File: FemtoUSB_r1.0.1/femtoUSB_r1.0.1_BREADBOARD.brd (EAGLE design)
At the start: 40.6 x 20.3 mm, 32 parts, among them IC1 ATSAMD21E18A-MUT

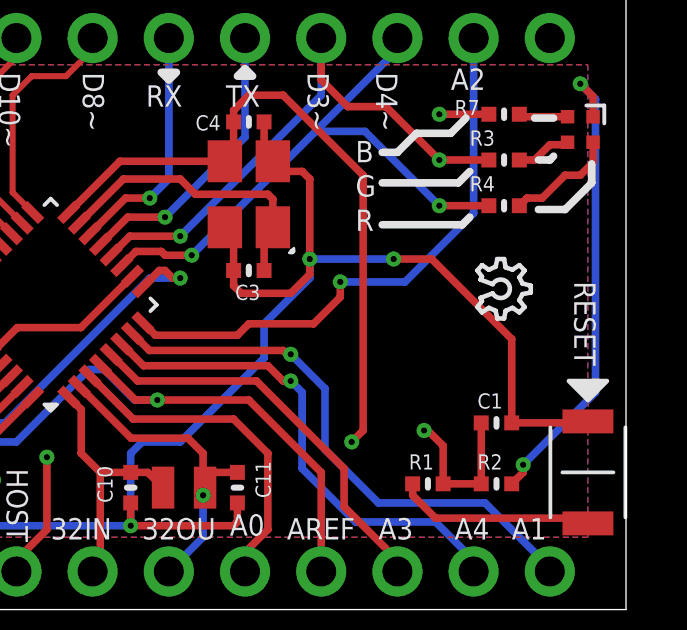
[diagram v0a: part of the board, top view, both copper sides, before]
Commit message: Updating FemtoUSB r1.0.1 w/ RGB. Silkscreen updated to reflect Arduino pin assignments
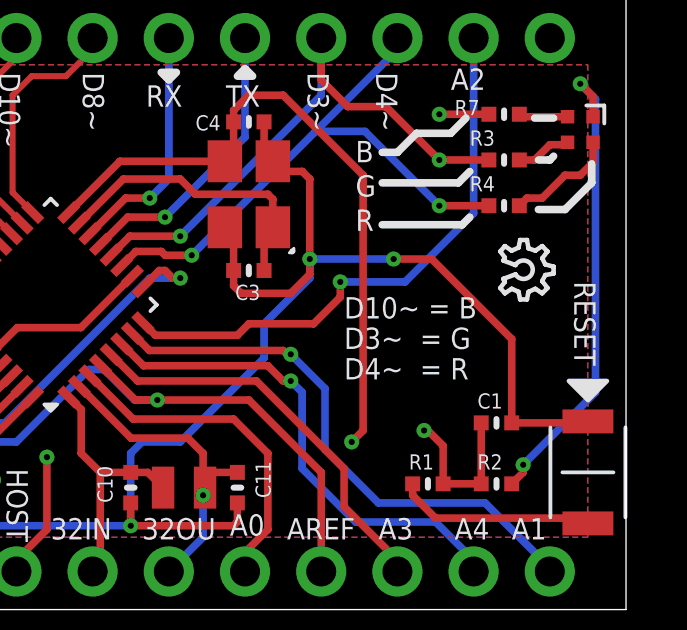
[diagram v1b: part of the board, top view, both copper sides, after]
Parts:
- moved OSH_LOGO 0.99 mm to (36.4, 12.3)
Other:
- board text added: "D10~ = B"
- board text added: "D3~ = G"
- board text added: "D4~ = R"
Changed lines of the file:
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@@
 <wire x1="38.1" y1="14.986" x2="38.227" y2="15.113" width="0.254" layer="25"/>
 <wire x1="37.592" y1="16.383" x2="38.227" y2="16.383" width="0.254" layer="25"/>
+<text x="31.242" y="10.414" size="0.7112" layer="25" font="vector" ratio="20" rot="SR0" align="top-left">D10~ = B</text>
+<text x="31.242" y="9.398" size="0.7112" layer="25" font="vector" ratio="20" rot="SR0" align="top-left">D3~  = G</text>
+<text x="31.242" y="8.382" size="0.7112" layer="25" font="vector" ratio="20" rot="SR0" align="top-left">D4~  = R</text>
 </plain>
 <attributes>
@@
 <attribute name="VALUE" x="11.303" y="14.8272" size="0.4572" layer="27" font="vector" ratio="20"/>
 </element>
-<element name="OSH_LOGO" library="ohw-logo" package="OSHW_6X70_NOTEXT" value="" x="35.687" y="11.684" rot="R270"/>
+<element name="OSH_LOGO" library="ohw-logo" package="OSHW_6X70_NOTEXT" value="" x="36.449" y="12.319" rot="R270"/>
 <element name="L1" library="microbuilder" package="_0603MP" value="10uH" x="11.557" y="4.318" smashed="yes" rot="R90">
 <attribute name="NAME" x="10.922" y="3.3655" size="0.508" layer="25" font="vector" ratio="20" rot="R90"/>
